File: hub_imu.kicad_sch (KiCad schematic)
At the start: 19 parts, among them J1 USB 1x4 P2.54, J2 SWD 2x3 P1.27, U1 STM32F042F6P6, U2 BNO055, U3 AP2112K-3.3

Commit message: Use JLCPCB basic parts; add "JLCPCB Part #" field to all parts
- Add a "JLCPCB Part #" field to every symbol/footprint, using codes
  confirmed as basic via JLCPCB's parts API (C1525, C52923, C23733,
  C25744, C25900, C11702, C2286, C5446). U1, U2, J1 and J2 are left
  blank (ICs not basic; headers hand-soldered).
- U3: AP2112K-3.3 (SOT-23-5, extended) -> XC6206P332MR (SOT-23-3, basic
  C5446). Pinout per Torex datasheet: 1 VSS, 2 VOUT, 3 VIN; the EN tie
  is removed. Rotated 180 deg so VIN faces J1/C1, and the corner re-routed.
- D1: 0402 LED -> 0603 red KT-0603R (basic C2286). R5/D1 shifted
  0.8 mm left so the cathode gets its own GND via.
- Refill pours, re-stitch; final DRC 0 errors / 0 unconnected.
- README: parts table with JLCPCB numbers, new U3/D1.

Co-Authored-By: Claude Opus 5.5 <noreply@anthropic.com>
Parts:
- C1: JLCPCB Part # (none) -> C52923
- C2: JLCPCB Part # (none) -> C23733
- C3, C4, C5, C6, C7, C8: JLCPCB Part # (none) -> C1525
- D1: footprint LED_SMD:LED_0402_1005Metric -> LED_SMD:LED_0603_1608Metric; JLCPCB Part # (none) -> C2286
- R1, R2: JLCPCB Part # (none) -> C25744
- R3, R4: JLCPCB Part # (none) -> C25900
- R5: JLCPCB Part # (none) -> C11702
- U3: value AP2112K-3.3 -> XC6206P332MR; footprint Package_TO_SOT_SMD:SOT-23-5 -> Package_TO_SOT_SMD:SOT-23-3; symbol hubimu:LDO_SOT23-5 -> hubimu:XC6206PxxxMR; JLCPCB Part # (none) -> C5446
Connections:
- net +3V3: now also U3.2 (VO); no longer U3.5 (VOUT)
- net +5V: no longer U3.1 (VIN)
- net GND: now also U3.1 (GND); no longer U3.2 (GND)
- no-connect marks 21 -> 20
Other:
- note added: "XC6206P332MR (JLCPCB basic C5446), SOT-23-3: 1 VSS, 2 VOUT, 3 VIN"
- note removed: "MIC5504-3.3YM5 / TLV70033 are pin-compatible"
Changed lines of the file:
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@@
 		)
 	)
-	(text "MIC5504-3.3YM5 / TLV70033 are pin-compatible"
+	(text "XC6206P332MR (JLCPCB basic C5446), SOT-23-3: 1 VSS, 2 VOUT, 3 VIN"
 		(exclude_from_sim no)
 		(at 15.24 95.25 0)
@@
 	)
 	(no_connect
-		(at 50.8 81.28)
-	)
-	(no_connect
 		(at 128.27 162.56)
 	)
@@
 	(wire
 		(pts
-			(xy 40.64 73.66) (xy 40.64 71.12)
-		)
-		(stroke
-			(width 0)
-			(type default)
-		)
-	)
-	(wire
-		(pts
 			(xy 71.12 124.46) (xy 71.12 123.19)
 		)
@@
 			)
 		)
+		(property "JLCPCB Part #" "C1525"
+			(at 118.11 111.76 0)
+			(effects
+				(font
+					(size 1.27 1.27)
+				)
+				(hide yes)
+			)
+		)
 		(pin "1"
 		)
@@
 			)
 		)
+		(property "JLCPCB Part #" "C1525"
+			(at 83.82 128.27 0)
+			(effects
+				(font
+					(size 1.27 1.27)
+				)
+				(hide yes)
+			)
+		)
 		(pin "1"
 		)
@@
 			)
 		)
+		(property "JLCPCB Part #" ""
+			(at 146.05 165.1 0)
+			(effects
+				(font
+					(size 1.27 1.27)
+				)
+				(hide yes)
+			)
+		)
 		(pin "11"
 		)
@@
 			)
 		)
+		(property "JLCPCB Part #" "C25744"
+			(at 195.58 167.64 0)
+			(effects
+				(font
+					(size 1.27 1.27)
+				)
+				(hide yes)
+			)
+		)
 		(pin "1"
 		)
@@
 			)
 		)
+		(property "JLCPCB Part #" "C1525"
+			(at 195.58 142.24 0)
+			(effects
+				(font
+					(size 1.27 1.27)
+				)
+				(hide yes)
+			)
+		)
 		(pin "1"
 		)
@@
 			)
 		)
+		(property "JLCPCB Part #" "C52923"
+			(at 17.78 81.28 0)
+			(effects
+				(font
+					(size 1.27 1.27)
+				)
+				(hide yes)
+			)
+		)
 		(pin "1"
 		)
@@
 			)
 		)
+		(property "JLCPCB Part #" "C25744"
+			(at 71.12 128.27 0)
+			(effects
+				(font
+					(size 1.27 1.27)
+				)
+				(hide yes)
+			)
+		)
 		(pin "1"
 		)
@@
 			)
 		)
+		(property "JLCPCB Part #" "C25900"
+			(at 208.28 167.64 0)
+			(effects
+				(font
+					(size 1.27 1.27)
+				)
+				(hide yes)
+			)
+		)
 		(pin "1"
 		)
@@
 			)
 		)
+		(property "JLCPCB Part #" "C1525"
+			(at 203.2 142.24 0)
+			(effects
+				(font
+					(size 1.27 1.27)
+				)
+				(hide yes)
+			)
+		)
 		(pin "1"
 		)
@@
 			)
 		)
-		(pin "1"
-		)
-		(pin "2"
-		)
-		(instances
-			(project "hub_imu"
-				(path "/3f2a9c1e-5b7d-4e8a-9c2f-1a6b8d4e7f01"
-					(reference "R4")
-					(unit 1)
-				)
-			)
-		)
-	)
-	(symbol
-		(lib_id "hubimu:+5V")
-		(at 40.64 71.12 0)
-		(unit 1)
-		(exclude_from_sim no)
-		(in_bom no)
-		(on_board no)
-		(dnp no)
-		(fields_autoplaced yes)
-		(property "Reference" "#PWR3"
-			(at 40.64 71.12 0)
-			(effects
-				(font
-					(size 1.27 1.27)
-				)
-				(hide yes)
-			)
-		)
-		(property "Value" "+5V"
-			(at 40.64 67.72 0)
-			(effects
-				(font
-					(size 1.27 1.27)
-				)
-			)
-		)
-		(property "Footprint" ""
-			(at 40.64 71.12 0)
-			(effects
-				(font
-					(size 1.27 1.27)
-				)
-				(hide yes)
-			)
-		)
-		(property "Datasheet" ""
-			(at 40.64 71.12 0)
-			(effects
-				(font
-					(size 1.27 1.27)
-				)
-				(hide yes)
-			)
-		)
-		(property "Description" ""
-			(at 40.64 71.12 0)
+		(property "JLCPCB Part #" "C25900"
+			(at 220.98 167.64 0)
 			(effects
 				(font
@@
 		(pin "1"
 		)
+		(pin "2"
+		)
 		(instances
 			(project "hub_imu"
 				(path "/3f2a9c1e-5b7d-4e8a-9c2f-1a6b8d4e7f01"
-					(reference "#PWR3")
+					(reference "R4")
 					(unit 1)
 				)
@@
 			)
 		)
+		(property "JLCPCB Part #" "C1525"
+			(at 110.49 111.76 0)
+			(effects
+				(font
+					(size 1.27 1.27)
+				)
+				(hide yes)
+			)
+		)
 		(pin "1"
 		)
@@
 			)
 		)
+		(property "JLCPCB Part #" "C23733"
+			(at 63.5 81.28 0)
+			(effects
+				(font
+					(size 1.27 1.27)
+				)
+				(hide yes)
+			)
+		)
 		(pin "1"
 		)
@@
 			)
 		)
+		(property "JLCPCB Part #" ""
+			(at 38.1 30.48 0)
+			(effects
+				(font
+					(size 1.27 1.27)
+				)
+				(hide yes)
+			)
+		)
 		(pin "1"
 		)
@@
 			)
 		)
+		(property "JLCPCB Part #" ""
+			(at 146.05 60.96 0)
+			(effects
+				(font
+					(size 1.27 1.27)
+				)
+				(hide yes)
+			)
+		)
 		(pin "17"
 		)
@@
 	)
 	(symbol
-		(lib_id "hubimu:LDO_SOT23-5")
-		(at 40.64 81.28 0)
+		(lib_id "hubimu:XC6206PxxxMR")
+		(at 40.64 78.74 0)
 		(unit 1)
 		(exclude_from_sim no)
@@
 			)
 		)
-		(property "Value" "AP2112K-3.3"
-			(at 33.02 86.32 0)
+		(property "Value" "XC6206P332MR"
+			(at 45.72 85.09 0)
 			(effects
 				(font
@@
 			)
 		)
-		(property "Footprint" "Package_TO_SOT_SMD:SOT-23-5"
+		(property "Footprint" "Package_TO_SOT_SMD:SOT-23-3"
 			(at 40.64 81.28 0)
 			(effects
@@
 			)
 		)
-		(property "Description" "3.3V 300-600mA LDO, SOT-23-5: 1 VIN, 2 GND, 3 EN, 4 NC, 5 VOUT"
+		(property "Description" "3.3V 200mA LDO, SOT-23-3: 1 VSS, 2 VOUT, 3 VIN"
 			(at 40.64 81.28 0)
 			(effects
@@
 			)
 		)
-		(pin "1"
+		(property "JLCPCB Part #" "C5446"
+			(at 40.64 78.74 0)
+			(effects
+				(font
+					(size 1.27 1.27)
+				)
+				(hide yes)
+			)
 		)
-		(pin "5"
+		(pin "1"
 		)
-		(pin "4"
+		(pin "2"
 		)
 		(pin "3"
 		)
-		(pin "2"
-		)
 		(instances
 			(project "hub_imu"
@@
 			)
 		)
+		(property "JLCPCB Part #" ""
+			(at 40.64 128.27 0)
+			(effects
+				(font
+					(size 1.27 1.27)
+				)
+				(hide yes)
+			)
+		)
 		(pin "1"
 		)
@@
 			)
 		)
+		(property "JLCPCB Part #" "C1525"
+			(at 220.98 142.24 0)
+			(effects
+				(font
+					(size 1.27 1.27)
+				)
+				(hide yes)
+			)
+		)
 		(pin "1"
 		)
@@
 			)
 		)
+		(property "JLCPCB Part #" "C11702"
+			(at 184.15 55.88 0)
+			(effects
+				(font
+					(size 1.27 1.27)
+				)
+				(hide yes)
+			)
+		)
 		(pin "1"
 		)
@@
 			)
 		)
-		(property "Footprint" "LED_SMD:LED_0402_1005Metric"
+		(property "Footprint" "LED_SMD:LED_0603_1608Metric"
 			(at 196.85 55.88 0)
 			(effects
@@
 			)
 		)
+		(property "JLCPCB Part #" "C2286"
+			(at 196.85 55.88 0)
+			(effects
+				(font
+					(size 1.27 1.27)
+				)
+				(hide yes)
+			)
+		)
 		(pin "1"
 		)
@@
 		)
 	)
+	(wire
+		(pts
+			(xy 30.48 78.74) (xy 33.02 78.74)
+		)
+		(stroke
+			(width 0)
+			(type default)
+		)
+	)
+	(wire
+		(pts
+			(xy 48.26 78.74) (xy 50.8 78.74)
+		)
+		(stroke
+			(width 0)
+			(type default)
+		)
+	)

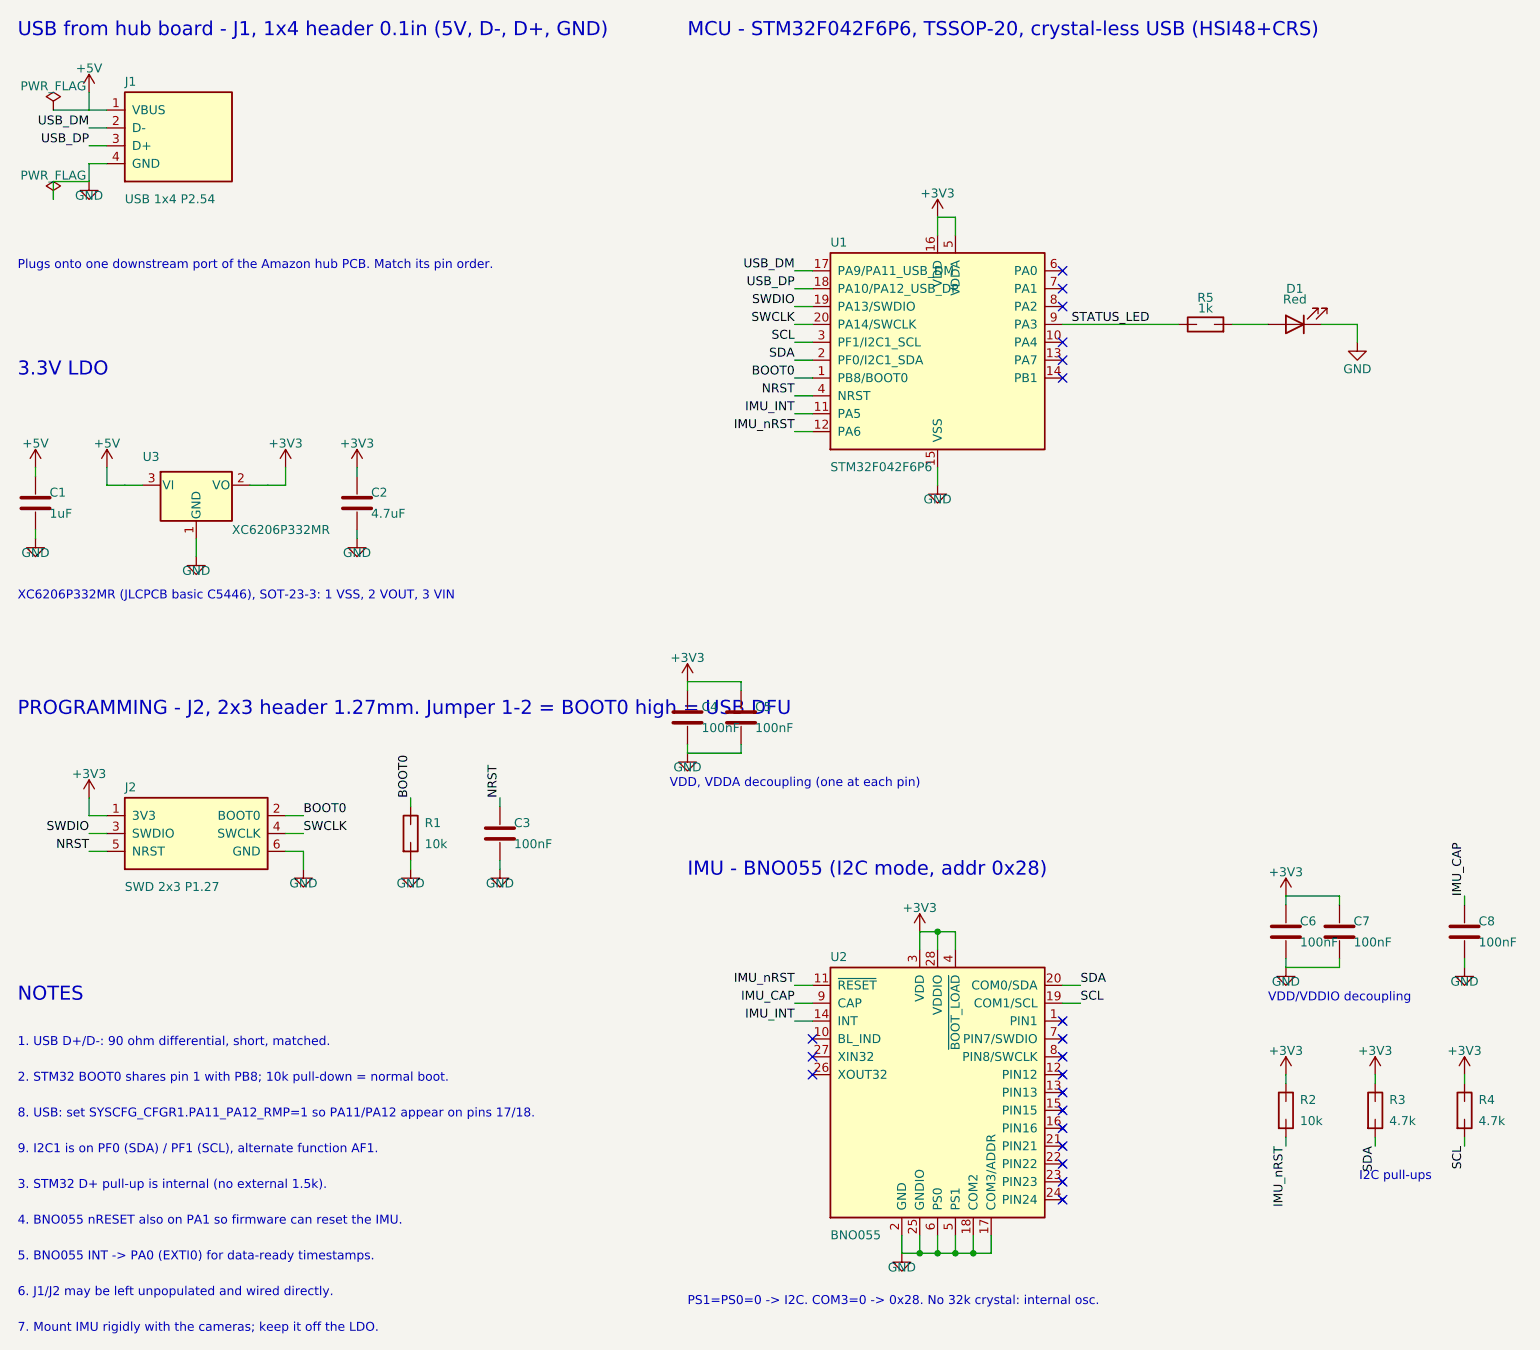
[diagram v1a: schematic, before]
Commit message: Board: EweFeel 1.0 back silkscreen, J1/J2 DNP, mask clearance 0.005 mm
Co-Authored-By: Claude Opus 5.5 <noreply@anthropic.com>
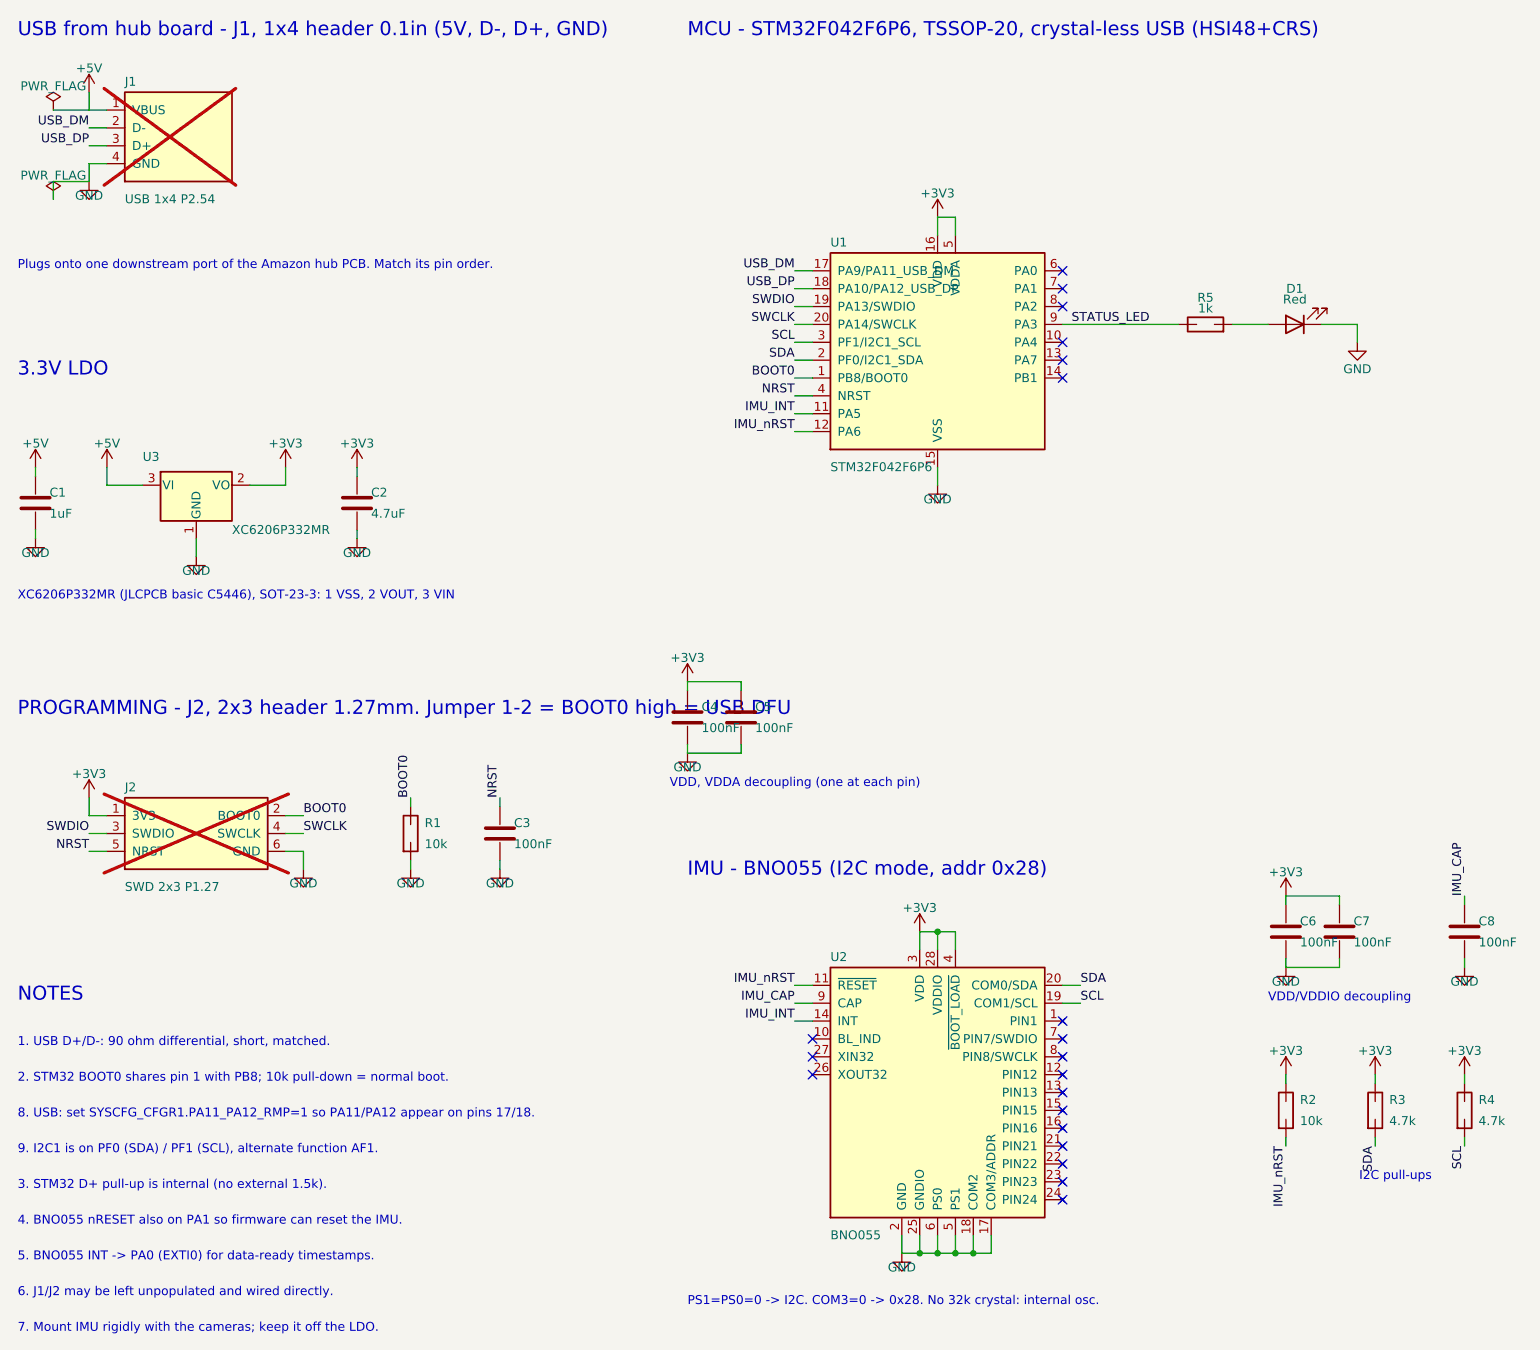
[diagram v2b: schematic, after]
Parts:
- J1, J2: now not fitted
